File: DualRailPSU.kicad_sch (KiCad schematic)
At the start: 19 parts, among them J1 Screw_Terminal_01x02, J2 1-726386-2, J3 Screw_Terminal_01x03

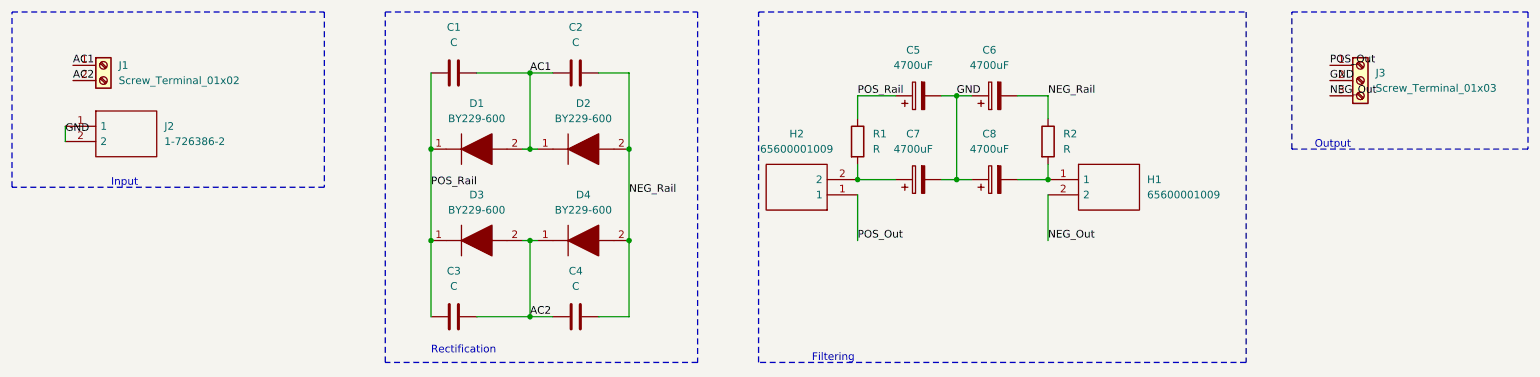
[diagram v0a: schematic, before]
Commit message: Fixed output terminal block orientation, and moved text and logo to silscreen front layer
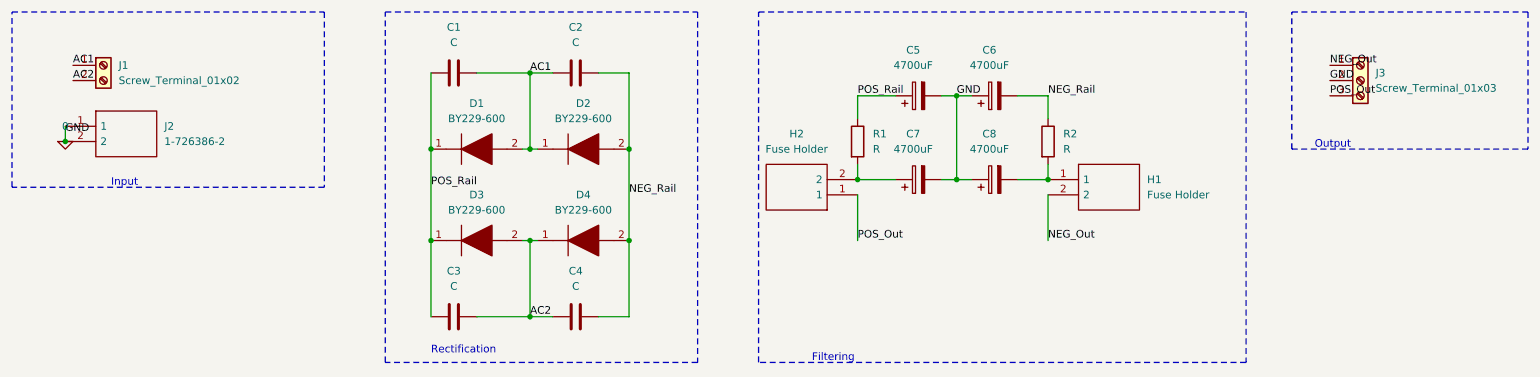
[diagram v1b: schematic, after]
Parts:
- H1, H2: value 65600001009 -> Fuse Holder
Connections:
- net NEG_Out: now also J3.1 (Pin_1); no longer J3.3 (Pin_3)
- net POS_Out: now also J3.3 (Pin_3); no longer J3.1 (Pin_1)
- net GND renamed 0
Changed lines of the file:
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@@
   (junction (at 172.72 54.61) (diameter 0) (color 0 0 0 0)
+  )
+  (junction (at 24.13 48.26) (diameter 0) (color 0 0 0 0)
   )
   (junction (at 187.96 54.61) (diameter 0) (color 0 0 0 0)
@@
     (effects (font (size 1.27 1.27)) (justify left bottom))
   )
+  (label "NEG_Out" (at 234.95 35.56 0) (fields_autoplaced)
+    (effects (font (size 1.27 1.27)) (justify left bottom))
+  )
   (label "NEG_Out" (at 187.96 64.77 0) (fields_autoplaced)
     (effects (font (size 1.27 1.27)) (justify left bottom))
   )
-  (label "POS_Out" (at 234.95 35.56 0) (fields_autoplaced)
-    (effects (font (size 1.27 1.27)) (justify left bottom))
-  )
   (label "AC1" (at 101.6 36.83 0) (fields_autoplaced)
     (effects (font (size 1.27 1.27)) (justify left bottom))
   )
-  (label "NEG_Out" (at 234.95 40.64 0) (fields_autoplaced)
+  (label "POS_Out" (at 234.95 40.64 0) (fields_autoplaced)
     (effects (font (size 1.27 1.27)) (justify left bottom))
   )
@@
       (effects (font (size 1.27 1.27)))
     )
-    (property "Value" "65600001009" (at 146.05 49.53 0)
+    (property "Value" "Fuse Holder" (at 146.05 49.53 0)
       (effects (font (size 1.27 1.27)))
     )
@@
       (effects (font (size 1.27 1.27)) (justify left))
     )
-    (property "Value" "65600001009" (at 204.47 57.15 0)
+    (property "Value" "Fuse Holder" (at 204.47 57.15 0)
       (effects (font (size 1.27 1.27)) (justify left))
     )
@@
         )
       )
+    )
+  )
+  (symbol (lib_id "Simulation_SPICE:0") (at 24.13 48.26 0) (unit 1)
+    (in_bom yes) (on_board yes) (dnp no) (fields_autoplaced)
+    (property "Reference" "#GND01" (at 24.13 50.8 0)
+      (effects (font (size 1.27 1.27)) hide)
+    )
+    (property "Value" "0" (at 24.13 45.72 0)
+      (effects (font (size 1.27 1.27)))
+    )
+    (property "Footprint" "" (at 24.13 48.26 0)
+      (effects (font (size 1.27 1.27)) hide)
+    )
+    (property "Datasheet" "~" (at 24.13 48.26 0)
+      (effects (font (size 1.27 1.27)) hide)
+    )
+    (pin "1")
+    (instances
+      (project "DualRailPSU"
+        (path "/a49c8600-a13e-4ddd-9f3c-2fba6b432c8b"
+          (reference "#GND01") (unit 1)
+        )
+      )
